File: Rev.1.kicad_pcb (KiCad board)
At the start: 4 copper layers, 238.3 x 170.8 mm, 228 parts, among them J1 Power from PowerBoard, J10 UnitV02, J11 GH-S37D, J12 NeoPixel, J13 LoadCell, J14 NeoPixel, J15 LoadCell, J16 Power to TopBoard, J17 Comm to TopBoard, J18 Conn_01x08_Socket, J19 ST-Link, J2 Power from PowerBoard, J20 USB_C_Receptacle_USB2.0_16P, J21 ST-Link, J22 to TopBoard, J23 LIDAR, J24 ST-Link, J25 to TopBoard, J26 Power to TopBoard, J27 Power to TopBoard, J28 Power to TopBoard, J29 Power from BackBoard, J3 ST-Link, J4 Power from PowerBoard, J5 Com from BackBoard, J6 to TileBoard, J7 to LidarBoard, J8 UnitV01, J9 GH-S37D, M1 STS3032, M2 STS3032, M3 STS3032, M4 STS3032, Q1 BSS138, Q2 BSS138, Q3 BSS138, Q4 BSS138, Q5 TJ15S06M3L, Q6 BSS138, Q7 BSS138, Q8 BSS138, SW1 RESET_SWITCH, SW10 MODE_SWITCH, SW11 TC-06104-043E, SW12 TC-06104-043E, SW2 MODE_SWITCH, SW3 GW-12LWP, SW4 RESET_SWITCH, SW5 MODE_SWITCH, SW6 START_SWITCH, SW7 RESET_SWITCH, SW8 MODE_SWITCH, SW9 RESET_SWITCH, U1 VL53L0X, U10 VL53L0X, U11 VL53L0X, U12 STM32F446RET6, U13 Sit2001B, U14 STM32F446RET6, U15 MAX3485, U16 Sit2001B, U17 RT9080-33GJ5, U18 Sit2001B, U19 STM32F446RET6, U2 Sit2001B, U20 S11059, U21 LT1085CM-3.3#PBF, U22 CH340E, U3 VL53L0X, U4 STM32H747IGT6, U5 AE-BNO055-BO, U6 NJU77551F, U7 NJU77551F, U8 MIC5219-5.0YM5-TR, U9 AZ1117CH-3.3TRG1

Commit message: LiDAR基板Rev.2修正
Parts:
- added J30: BNO055, Connector_PinSocket_1.27mm:PinSocket_1x02_P1.27mm_Vertical, F.Cu at (71.8, 132.5)
- added J31: UNITV, Connector_PinSocket_1.27mm:PinSocket_1x02_P1.27mm_Vertical, F.Cu at (66.8, 132.5)
- added J32: UNITV, Connector_PinSocket_1.27mm:PinSocket_1x02_P1.27mm_Vertical, F.Cu at (46.2, 122.3)
- added J33: to TileBoard, Connector_PinSocket_1.27mm:PinSocket_1x02_P1.27mm_Vertical, F.Cu at (56.9, 129.1)
- added J34: SERVO, Connector_PinSocket_1.27mm:PinSocket_1x02_P1.27mm_Vertical, F.Cu at (53.8, 111.4)
- added J35: NeoPixel, Connector_PinSocket_1.27mm:PinSocket_1x02_P1.27mm_Vertical, F.Cu at (46.2, 117.6)
- added R34: 680, Resistor_SMD:R_0603_1608Metric, F.Cu at (154.5, 135.3)
- added R48: 10k, Resistor_SMD:R_0603_1608Metric, F.Cu at (198.5, 146.0)
- added U23: AE-BNO055-BO, AE-BNO055-BO:AE-BNO055-BO, F.Cu at (125.7, 134.6)
- C43, R21, R22, SW4, SW5: moved to F.Cu
- moved SW4 102.6 mm to (251.6, 138.9), turned to 0 degrees
- moved J21 96.2 mm to (215.4, 154.9), turned to -90 degrees
- moved C43 95.0 mm to (247.8, 139.3)
- moved R22 88.8 mm to (244.1, 142.0), turned to 180 degrees
- moved SW5 82.5 mm to (240.9, 138.1), turned to 0 degrees
- moved R21 75.8 mm to (237.6, 142.0), turned to 180 degrees
- moved SW8 55.0 mm to (240.7, 146.5)
- moved R28 52.4 mm to (237.1, 150.8)
- moved R29 44.9 mm to (244.2, 151.0), turned to 180 degrees
- moved C51 43.2 mm to (322.2, 141.0), turned to -90 degrees
- moved SW7 41.7 mm to (251.8, 146.7)
- moved C50 40.6 mm to (318.7, 152.2), turned to 180 degrees
- moved C54 36.6 mm to (247.5, 146.8), turned to -90 degrees
- moved C56 34.5 mm to (316.8, 154.3)
- moved U14 33.9 mm to (313.4, 144.2)
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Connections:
- C58 pad 2: Net-(U22-VCC) -> Net-(U22-V3)
- SW11 pad 2: Net-(U19-PC6) -> Net-(U19-PB12)
- SW12 pad 2: Net-(U19-PC7) -> Net-(U19-PB13)
- U14 pad 21: unconnected-(U14-PA5-Pad21) -> /Back/SCK
- U14 pad 22: unconnected-(U14-PA6-Pad22) -> /Back/MOSI
- U14 pad 23: unconnected-(U14-PA7-Pad23) -> /Back/MISO
- U14 pad 41: unconnected-(U14-PA8-Pad41) -> /Back/CS
- U19 pad 22: unconnected-(U19-PA6-Pad22) -> /Lidar/PWM
- U19 pad 23: unconnected-(U19-PA7-Pad23) -> /Lidar/PWM2
- U19 pad 33: unconnected-(U19-PB12-Pad33) -> Net-(U19-PB12)
- U19 pad 34: unconnected-(U19-PB13-Pad34) -> Net-(U19-PB13)
- U19 pad 35: unconnected-(U19-PB14-Pad35) -> /Lidar/IN2
- U19 pad 36: unconnected-(U19-PB15-Pad36) -> /Lidar/IN3
- U19 pad 37: Net-(U19-PC6) -> /Lidar/TX6
- U19 pad 38: Net-(U19-PC7) -> /Lidar/RX6
- U19 pad 40: unconnected-(U19-PC9-Pad40) -> /Lidar/SDA2
- U19 pad 41: unconnected-(U19-PA8-Pad41) -> /Lidar/SCL2
- U19 pad 53: unconnected-(U19-PC12-Pad53) -> /Lidar/TX5
- U19 pad 54: unconnected-(U19-PD2-Pad54) -> /Lidar/RX5
- U19 pad 58: unconnected-(U19-PB6-Pad58) -> /Lidar/SCL
- U19 pad 59: unconnected-(U19-PB7-Pad59) -> /Lidar/SDA
- U22 pad 10: +5V -> Net-(U22-V3)
- U22 pad 7: Net-(U22-VCC) -> +5V
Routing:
- net Net-(M1-S): track 184.2 -> 0.00 mm
- net +3.3V: track 494.3 -> 374.4 mm, vias 72 -> 53
- net GND: track 694.0 -> 585.1 mm, vias 512 -> 432
- net /Back/NRST: track 108.4 -> 0.00 mm, vias 3 -> 0
- net /Back/SDA: track 98.4 -> 0.00 mm
- net +7.5V: track 416.9 -> 332.7 mm, vias 5 -> 0
- net /Back/SCL: track 77.3 -> 0.00 mm
- net Net-(SW5A-B): track 62.8 -> 0.00 mm, vias 2 -> 0
- net Net-(BT1-+): track 66.5 -> 8.54 mm, vias 1 -> 0
- net +5V: track 632.9 -> 586.0 mm, vias 14 -> 10
- net /Back/XSHUT2: track 43.9 -> 0.00 mm
- net /Back/XSHUT1: track 33.1 -> 0.00 mm, vias 1 -> 0
- net /Back/TX3: track 32.1 -> 0.00 mm, vias 2 -> 0
- net /Back/DIN: track 32.0 -> 0.00 mm
- net /Back/PC2: track 30.1 -> 0.00 mm, vias 2 -> 0
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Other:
- board text added: "BNO055"
- board text added: "C"
- board text added: "D"
- board text added: "NeoPixel"
- board text added: "R"
- board text added: "SERVO"
- board text added: "T"
- board text added: "Tile"
- board text added: "UNITV"

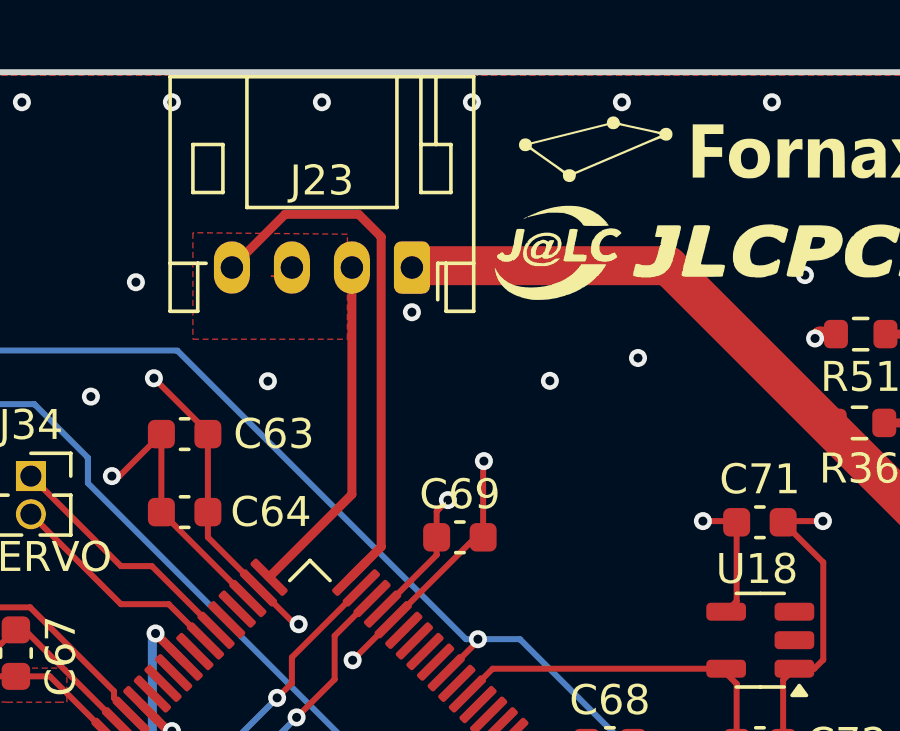
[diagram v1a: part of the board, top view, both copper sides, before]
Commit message: LiDAR基板Rev.2修正v2
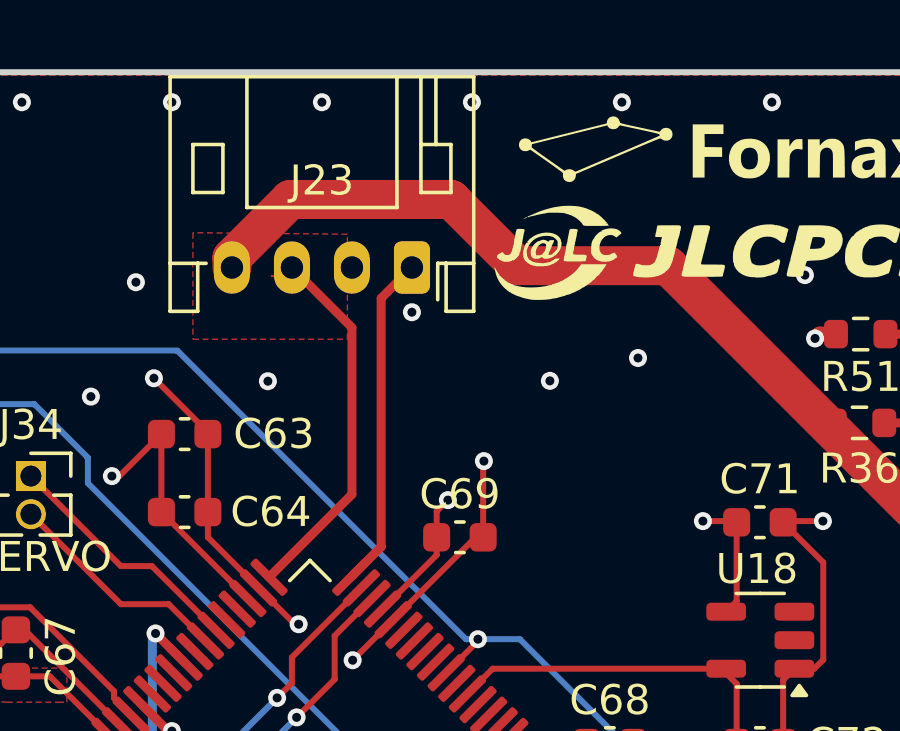
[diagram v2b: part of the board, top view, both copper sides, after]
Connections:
- J23 pad 1: +5V -> /Lidar/TX2
- J23 pad 2: /Lidar/RX2 -> GND
- J23 pad 3: GND -> /Lidar/RX2
- J23 pad 4: /Lidar/TX2 -> +5V
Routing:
- net +5V: track 586.0 -> 594.6 mm
- net /Lidar/TX2: track 18.1 -> 11.2 mm
- net /Lidar/RX2: track 11.6 -> 12.5 mm
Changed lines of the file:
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@@
 			(remove_unused_layers no)
 			(roundrect_rratio 0.208333)
-			(net 4 "+5V")
+			(net 17 "/Lidar/TX2")
 			(pinfunction "Pin_1")
 			(pintype "passive")
@@
 			(layers "*.Cu" "*.Mask")
 			(remove_unused_layers no)
-			(net 18 "/Lidar/RX2")
+			(net 3 "GND")
 			(pinfunction "Pin_2")
 			(pintype "passive")
@@
 			(layers "*.Cu" "*.Mask")
 			(remove_unused_layers no)
-			(net 3 "GND")
+			(net 18 "/Lidar/RX2")
 			(pinfunction "Pin_3")
 			(pintype "passive")
@@
 			(layers "*.Cu" "*.Mask")
 			(remove_unused_layers no)
-			(net 17 "/Lidar/TX2")
+			(net 4 "+5V")
 			(pinfunction "Pin_4")
 			(pintype "passive")
@@
 	)
 	(segment
+		(start 75.039666 104.387132)
+		(end 70.017132 104.387132)
+		(width 1.3)
+		(layer "F.Cu")
+		(net 4)
+	)
+	(segment
 		(start 40.780367 137.306717)
 		(end 40.780367 138.777632)
@@
 	)
 	(segment
-		(start 93.250367 137.729132)
-		(end 93.250367 121.687132)
-		(width 1.3)
-		(layer "F.Cu")
-		(net 4)
-	)
-	(segment
-		(start 93.250367 121.687132)
-		(end 86.263235 114.7)
-		(width 1.3)
-		(layer "F.Cu")
-		(net 4)
-	)
-	(segment
 		(start 90.5 180.05)
 		(end 91.3 180.85)
@@
 	)
 	(segment
+		(start 93.208367 137.729132)
+		(end 93.250367 137.729132)
+		(width 1.3)
+		(layer "F.Cu")
+		(net 4)
+	)
+	(segment
 		(start 64.075367 140.437132)
 		(end 64.075367 139.910526)
@@
 	)
 	(segment
-		(start 75.039666 104.387132)
-		(end 66.560367 104.387132)
+		(start 93.250367 121.687132)
+		(end 86.263235 114.7)
 		(width 1.3)
 		(layer "F.Cu")
@@
 	)
 	(segment
-		(start 56.573 64.778)
-		(end 56.4665 64.8845)
-		(width 1.5)
+		(start 60.410367 104.387132)
+		(end 60.560367 104.387132)
+		(width 0.3)
 		(layer "F.Cu")
 		(net 4)
 	)
 	(segment
-		(start 93.208367 137.729132)
-		(end 93.250367 137.729132)
+		(start 70.017132 104.387132)
+		(end 67.81 102.18)
 		(width 1.3)
 		(layer "F.Cu")
@@
 	)
 	(segment
+		(start 56.573 64.778)
+		(end 56.4665 64.8845)
+		(width 1.5)
+		(layer "F.Cu")
+		(net 4)
+	)
+	(segment
 		(start 48.687867 127.362133)
 		(end 48.687867 131.02)
@@
 	)
 	(segment
+		(start 93.250367 137.729132)
+		(end 93.250367 121.687132)
+		(width 1.3)
+		(layer "F.Cu")
+		(net 4)
+	)
+	(segment
 		(start 230.35 74.35)
 		(end 230.35 75.6)
@@
 	)
 	(segment
+		(start 60.500367 104.887132)
+		(end 60.500367 104.597128)
+		(width 0.2)
+		(layer "F.Cu")
+		(net 4)
+	)
+	(segment
 		(start 53.9655 65.8125)
 		(end 53.0375 64.8845)
@@
 	)
 	(segment
+		(start 60.500367 104.121522)
+		(end 60.500367 104.447132)
+		(width 1.3)
+		(layer "F.Cu")
+		(net 4)
+	)
+	(segment
 		(start 62.8125 65.8125)
 		(end 72.5725 75.5725)
@@
 	)
 	(segment
+		(start 65.300367 145.037132)
+		(end 85.900367 145.037132)
+		(width 1.3)
+		(layer "F.Cu")
+		(net 4)
+	)
+	(segment
 		(start 50.650367 131.024632)
 		(end 48.692499 131.024632)
@@
 	)
 	(segment
+		(start 67.81 102.18)
+		(end 62.441889 102.18)
+		(width 1.3)
+		(layer "F.Cu")
+		(net 4)
+	)
+	(segment
 		(start 253.745 63.345)
 		(end 254.1 63.7)
@@
 	)
 	(segment
+		(start 62.441889 102.18)
+		(end 60.500367 104.121522)
+		(width 1.3)
+		(layer "F.Cu")
+		(net 4)
+	)
+	(segment
+		(start 85.352534 114.7)
+		(end 75.039666 104.387132)
+		(width 1.3)
+		(layer "F.Cu")
+		(net 4)
+	)
+	(segment
 		(start 48.687867 131.02)
 		(end 48.687867 133.912867)
@@
 	)
 	(segment
-		(start 65.300367 145.037132)
-		(end 85.900367 145.037132)
-		(width 1.3)
-		(layer "F.Cu")
-		(net 4)
-	)
-	(segment
 		(start 91.3 180.85)
 		(end 99.15 180.85)
@@
 	)
 	(segment
-		(start 86.263235 114.7)
-		(end 85.352534 114.7)
+		(start 85.900367 145.037132)
+		(end 93.208367 137.729132)
 		(width 1.3)
 		(layer "F.Cu")
@@
 	)
 	(segment
-		(start 85.900367 145.037132)
-		(end 93.208367 137.729132)
+		(start 86.263235 114.7)
+		(end 85.352534 114.7)
 		(width 1.3)
 		(layer "F.Cu")
@@
 	)
 	(segment
-		(start 85.352534 114.7)
-		(end 75.039666 104.387132)
-		(width 1.3)
-		(layer "F.Cu")
-		(net 4)
-	)
-	(segment
 		(start 84.975367 133.499632)
 		(end 84.975367 124.781371)
@@
 	)
 	(segment
-		(start 60.410367 104.387132)
-		(end 60.560367 104.387132)
+		(start 66.500367 104.447132)
+		(end 65.475367 105.472132)
 		(width 0.3)
 		(layer "F.Cu")
@@
 	)
 	(segment
-		(start 64.725367 102.674632)
-		(end 65.475367 103.424632)
-		(width 0.3)
-		(layer "F.Cu")
-		(net 17)
-	)
-	(segment
-		(start 62.272867 102.674632)
-		(end 64.725367 102.674632)
-		(width 0.3)
-		(layer "F.Cu")
-		(net 17)
-	)
-	(segment
-		(start 60.560367 104.387132)
-		(end 62.272867 102.674632)
+		(start 65.475367 105.472132)
+		(end 65.475367 113.758832)
 		(width 0.3)
 		(layer "F.Cu")
@@
 	)
 	(segment
-		(start 60.500367 104.887132)
-		(end 60.500367 104.597128)
-		(width 0.2)
-		(layer "F.Cu")
-		(net 17)
-	)
-	(segment
 		(start 65.475367 113.758832)
 		(end 64.461548 114.772651)
@@
 	)
 	(segment
-		(start 65.475367 103.424632)
-		(end 65.475367 113.758832)
+		(start 62.650367 104.297132)
+		(end 62.500367 104.447132)
 		(width 0.3)
 		(layer "F.Cu")
-		(net 17)
+		(net 18)
 	)
 	(segment
-		(start 64.500367 104.447132)
-		(end 64.500367 112.01147)
+		(start 62.500367 104.447132)
+		(end 64.500367 106.447132)
 		(width 0.3)
 		(layer "F.Cu")
@@
 	)
 	(segment
-		(start 64.500367 104.297132)
-		(end 64.500367 104.447132)
+		(start 64.500367 106.447132)
+		(end 64.500367 112.01147)
 		(width 0.3)
 		(layer "F.Cu")

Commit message: メイン基板Rev.2完成
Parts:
- removed the C18 at (225.5, 48.7)
- removed the C19 at (225.5, 44.7)
- removed the C22 at (225.5, 32.5)
- removed the C23 at (189.1, 56.7)
- removed the C24 at (186.6, 56.7)
- removed the C25 at (158.8, 77.5)
- removed the C26 at (186.6, 52.6)
- removed the C27 at (189.1, 52.6)
- removed the C30 at (201.9, 27.5)
- removed the C31 at (222.2, 27.5)
- removed the J12 at (255.8, 49.5)
- removed the J14 at (158.0, 49.5)
- removed the Q3 at (254.7, 56.8)
- removed the Q4 at (161.9, 55.2)
- removed Q7: BSS138, Package_TO_SOT_SMD:SOT-23
- removed the R10 at (255.2, 53.5)
- removed the R15 at (156.8, 55.5)
- removed the R16 at (167.2, 51.7)
- removed the R23 at (255.4, 122.2)
- removed the R9 at (257.3, 60.0)
- removed the SW6 at (245.6, 126.6)
- removed the U10 at (181.6, 150.3)
- added D4: LED, LED_SMD:LED_0603_1608Metric, F.Cu at (208.9, 154.5)
- added G***: LOGO, icon:fornax-logo-pcb15-3.8, F.Cu at (167.2, 23.4)
- added G***: LOGO, icon:jlcpcb-logo-pcb15-8, F.Cu at (167.2, 26.7)
- added Q5: BSS138, Package_TO_SOT_SMD:SOT-23, F.Cu at (261.7, 120.7)
- added R18: 470, Resistor_SMD:R_0603_1608Metric, F.Cu at (205.3, 154.6)
- added R19: 1k, Resistor_SMD:R_0603_1608Metric, F.Cu at (167.9, 141.3)
- added R25: 10k, Capacitor_SMD:C_0603_1608Metric_Pad1.08x0.95mm_HandSolder, F.Cu at (257.1, 122.0)
- added SW3: B-12CCP, B-12CCP:B-12CCP, F.Cu at (172.3, 136.7)
- added U13: ~, Connector_PinSocket_2.54mm:PinSocket_1x06_P2.54mm_Vertical, F.Cu at (234.8, 160.5)
- added U7: MOUDLE-SEEEDUINO-XIAO-ESP32C3, XIAO:MOUDLE14P-SMD-2.54-21X17.8MM, F.Cu at (269.0, 64.3)
- C1, C15: value 0.1uF -> 1uF
- C14: value 0.1uF -> 4.7uF
- C20, C21: value 0.1uF -> 2.2uF
- FB1: footprint Capacitor_SMD:C_0603_1608Metric -> Inductor_SMD:L_0603_1608Metric
- J11, J9: footprint Connector_PinHeader_2.54mm:PinHeader_1x03_P2.54mm_Vertical -> Connector_JST:JST_ZH_B3B-ZR_1x03_P1.50mm_Vertical
- J6: moved to B.Cu
- R1, R2: footprint Resistor_SMD:R_0603_1608Metric -> Capacitor_SMD:C_0603_1608Metric_Pad1.08x0.95mm_HandSolder
- R26: value 10k -> 1k; footprint Capacitor_SMD:C_0603_1608Metric_Pad1.08x0.95mm_HandSolder -> Resistor_SMD:R_0603_1608Metric
- R3: value 10k -> 47
- R31, R32, U5: moved to F.Cu
- R4: value 0 -> 10k; footprint Resistor_SMD:R_0603_1608Metric -> Capacitor_SMD:C_0603_1608Metric_Pad1.08x0.95mm_HandSolder
- SW6: renamed from SW3; value GW-12LWP -> B-12CCP; footprint GW-12LWP:GW-12LWP -> B-12CCP:B-12CCP
- U1, U11, U3: value VL53L0X -> ~; footprint Connector_PinHeader_2.54mm:PinHeader_1x05_P2.54mm_Vertical -> Connector_PinSocket_2.54mm:PinSocket_1x06_P2.54mm_Vertical
- U4: value STM32H747IGT6 -> STM32H723ZGTx; footprint Package_QFP:LQFP-176_24x24mm_P0.5mm -> Package_QFP:LQFP-144_20x20mm_P0.5mm
- moved U3 123.9 mm to (273.1, 76.1), turned to 180 degrees
- moved U1 118.3 mm to (149.0, 63.5), turned to 0 degrees
- moved R2 108.1 mm to (256.1, 23.4), turned to 180 degrees
- moved SW1 106.8 mm to (252.8, 36.4)
- moved C47 106.4 mm to (196.6, 107.5)
- moved U17 106.4 mm to (196.5, 111.3)
- moved C42 106.1 mm to (202.7, 112.4), turned to 180 degrees
- moved C45 106.0 mm to (196.6, 114.7)
- moved SW2 105.8 mm to (252.7, 28.2), turned to 0 degrees
- moved C39 105.4 mm to (208.3, 125.9)
- moved C43 105.4 mm to (207.8, 109.0)
- moved C40 105.4 mm to (216.8, 125.3)
- moved C41 105.4 mm to (220.3, 114.1)
- moved C37 105.4 mm to (207.9, 105.8)
- moved C38 105.4 mm to (202.5, 118.9)
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- renumbered C28 to C18, C29 to C19, C32 to C22, C33 to C23, C34 to C24, C35 to C25, C36 to C26, C37 to C27, C38 to C28, C39 to C29, C40 to C30, C41 to C31, C42 to C32, C43 to C33, C44 to C34, C45 to C35, C46 to C36, C47 to C37, C48 to C38, C49 to C39, C50 to C40, C51 to C41, C52 to C42, C53 to C43, C54 to C44, C55 to C45, C59 to C46, C57 to C47, C56 to C48, C63 to C49, C64 to C50, C65 to C51, C66 to C52, C67 to C53, C68 to C54, C69 to C55, C62 to C56, C61 to C57, C70 to C58, C60 to C59, C58 to C60, C71 to C61, C73 to C62, C72 to C63, C74 to C64, C75 to C65, C76 to C66, C77 to C67, C78 to C68, D8 to D10, D9 to D11, D10 to D12, D11 to D13, D4 to D5, D5 to D6, D6 to D7, D7 to D8, D12 to D9, J13 to J12, J15 to J13, J16 to J14, J17 to J15, J18 to J16, J19 to J17, J21 to J18, J24 to J19, J22 to J20, J20 to J21, J23 to J22, J30 to J23, J31 to J24, J33 to J25, J32 to J26, J34 to J27, J35 to J28, J25 to J29, J26 to J30, J27 to J31, J28 to J32, J29 to J33, MD2 to MD1, Q5 to Q3, Q6 to Q4, Q8 to Q6, R12 to R10, R13 to R11, R14 to R12, R17 to R13, R18 to R14, R19 to R15, R20 to R16, R48 to R17, R21 to R20, R22 to R21, R34 to R22, R25 to R23, R35 to R34, R36 to R35, R37 to R36, R38 to R37, R49 to R38, R50 to R39, R51 to R40, R39 to R41, R40 to R42, R41 to R43, R42 to R44, R43 to R45, R44 to R46, R45 to R47, R46 to R48, R47 to R49, R11 to R9, U9 to U10, U23 to U12, U12 to U14, U13 to U15, U14 to U16, U16 to U17, U15 to U18, U17 to U19, U22 to U20, U19 to U21, U18 to U22, U20 to U23, U21 to U24, U7 to U8, U8 to U9
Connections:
- C15 pad 1: +3.3V -> VDDA
- C16 pad 1: +3.3V -> VDDA
- C17 pad 1: +3.3V -> GND
- C17 pad 2: GND -> /Top/NRST
- C20 pad 1: +3.3V -> GND
- C20 pad 2: GND -> Net-(C20-Pad2)
- C21 pad 1: +3.3V -> GND
- C21 pad 2: GND -> Net-(C21-Pad2)
- J22 pad 1: /Lidar/TX2 -> +5V
- J22 pad 2: GND -> /Lidar/RX2
- J22 pad 3: /Lidar/RX2 -> GND
- J22 pad 4: +5V -> /Lidar/TX2
- Q3 pad 2: Net-(Q5-G) -> Net-(Q3-G)
- R1 pad 2: Net-(U4-PDR_ON) -> Net-(SW2A-A)
- R17 pad 1: Net-(Q5-G) -> Net-(Q3-G)
- R2 pad 1: +3.3V -> GND
- R2 pad 2: Net-(SW2A-A) -> Net-(SW2A-C)
- R23 pad 2: Net-(SW6A-A) -> Net-(R23-Pad2)
- R24 pad 1: +3.3V -> +5V
- R26 pad 1: GND -> Net-(R26-Pad1)
- R26 pad 2: Net-(SW6A-C) -> +7.5V
- R3 pad 1: GND -> VDDA
- R3 pad 2: Net-(SW2A-C) -> Net-(U4-VREF+)
- R4 pad 1: VDDA -> +3.3V
- R4 pad 2: Net-(U4-VREF+) -> Net-(U4-PDR_ON)
- R7 pad 2: /Top/DIN1 -> Net-(D1-DIN)
- R8 pad 2: Net-(D1-DIN) -> /Top/DIN1
- SW6 pad 1: Net-(Q5-G) -> Net-(R23-Pad2)
- SW6 pad 2: GND -> Net-(SW6-B)
- SW6 pad 3: unconnected-(SW3A-C-Pad3) -> GND
- U1 pad 1: /Top/XSHUT1 -> unconnected-(U1-GPIO1-Pad1)
- U1 pad 2: +3.3V -> /Top/XSHUT1
- U1 pad 3: GND -> +3.3V
- U1 pad 4: /Top/SDA -> GND
- U1 pad 5: /Top/SCL -> /Top/SDA
- U11 pad 1: /Back/XSHUT1 -> unconnected-(U11-GPIO1-Pad1)
- U11 pad 2: +3.3V -> /Back/XSHUT2
- U11 pad 3: GND -> +3.3V
- U11 pad 4: /Back/SDA -> GND
- U11 pad 5: /Back/SCL -> /Back/SDA
- U14 pad 33: Net-(SW6A-B) -> Net-(SW6-B)
- U16 pad 26: unconnected-(U14-PB0-Pad26) (its old number) -> /Back/DC
- U16 pad 27: unconnected-(U14-PB1-Pad27) (its old number) -> /Back/PWM
- U16 pad 28: unconnected-(U14-PB2-Pad28) (its old number) -> /Back/DIN
- U3 pad 1: /Top/XSHUT2 -> unconnected-(U3-GPIO1-Pad1)
- U3 pad 2: +3.3V -> /Top/XSHUT2
- U3 pad 3: GND -> +3.3V
- U3 pad 4: /Top/SDA -> GND
- U3 pad 5: /Top/SCL -> /Top/SDA
- U4 pad 100: GND -> unconnected-(U4-PA8-Pad100)
- U4 pad 101: +3.3V -> unconnected-(U4-PA9-Pad101)
- U4 pad 102: +3.3V -> unconnected-(U4-PA10-Pad102)
- U4 pad 103: GND -> unconnected-(U4-PA11-Pad103)
- U4 pad 104: GND -> unconnected-(U4-PA12-Pad104)
- U4 pad 105: GND -> /Top/SWDIO
- U4 pad 106: GND -> Net-(C21-Pad2)
- U4 pad 109: GND -> /Top/SWCLK
- U4 pad 112: GND -> unconnected-(U4-PC11-Pad112)
- U4 pad 113: +3.3V -> unconnected-(U4-PC12-Pad113)
- U4 pad 119: GND -> unconnected-(U4-PD5-Pad119)
- U4 pad 12: GND -> unconnected-(U4-PF2-Pad12)
- U4 pad 120: unconnected-(U4-VDD50_USB-Pad120) -> GND
- U4 pad 121: GND -> +3.3V
- U4 pad 122: /Top/TX6 -> unconnected-(U4-PD6-Pad122)
- U4 pad 123: /Top/RX6 -> unconnected-(U4-PD7-Pad123)
- U4 pad 126: +3.3V -> unconnected-(U4-PG11-Pad126)
- U4 pad 13: +3.3V -> unconnected-(U4-PF3-Pad13)
- U4 pad 130: unconnected-(U4-PA11-Pad130) -> GND
- U4 pad 131: unconnected-(U4-PA12-Pad131) -> +3.3V
- U4 pad 132: /Top/SWDIO -> unconnected-(U4-PG15-Pad132)
- U4 pad 133: Net-(C30-Pad2) -> unconnected-(U4-PB3(JTDO-Pad133)
- U4 pad 134: GND -> unconnected-(U4-PB4(NJTRST)-Pad134)
- U4 pad 135: +3.3V -> unconnected-(U4-PB5-Pad135)
- U4 pad 136: +3.3V -> unconnected-(U4-PB6-Pad136)
- U4 pad 137: GND -> unconnected-(U4-PB7-Pad137)
- U4 pad 138: /Top/SWCLK -> Net-(SW2A-B)
- U4 pad 14: GND -> unconnected-(U4-PF4-Pad14)
- U4 pad 143: unconnected-(U4-PD0-Pad143) -> Net-(U4-PDR_ON)
- U4 pad 144: unconnected-(U4-PD1-Pad144) -> +3.3V
- U4 pad 15: GND -> unconnected-(U4-PF5-Pad15)
- U4 pad 17: GND -> +3.3V
- U4 pad 18: unconnected-(U4-PF0-Pad18) -> /Top/RX7
- U4 pad 19: unconnected-(U4-PF1-Pad19) -> /Top/TX7
- U4 pad 23: unconnected-(U4-PF5-Pad23) -> /Top/HSE
- U4 pad 24: GND -> unconnected-(U4-PH1-Pad24)
- U4 pad 25: +3.3V -> /Top/NRST
- U4 pad 28: /Top/DIN3 -> unconnected-(U4-PC2_C-Pad28)
- U4 pad 30: unconnected-(U4-PF10-Pad30) -> +3.3V
- U4 pad 31: /Top/HSE -> GND
- U4 pad 32: unconnected-(U4-PH1-Pad32) -> Net-(U4-VREF+)
- U4 pad 33: /Top/NRST -> VDDA
- U4 pad 34: unconnected-(U4-PC0-Pad34) -> /Top/TX4
- U4 pad 35: unconnected-(U4-PC1-Pad35) -> /Top/RX4
- U4 pad 36: unconnected-(U4-PC2_C-Pad36) -> /Top/TX2
- U4 pad 37: unconnected-(U4-PC3_C-Pad37) -> /Top/RX2
- U4 pad 39: Net-(U4-VREF+) -> +3.3V
- U4 pad 40: VDDA -> unconnected-(U4-PA4-Pad40)
- U4 pad 41: /Top/TX4 -> /Top/PWM2
- U4 pad 42: /Top/RX4 -> /Top/DIN1
- U4 pad 43: /Top/TX2 -> unconnected-(U4-PA7-Pad43)
- U4 pad 44: +3.3V -> /Top/AD1
- U4 pad 45: GND -> unconnected-(U4-PC5-Pad45)
- U4 pad 46: /Top/RX2 -> unconnected-(U4-PB0-Pad46)
- U4 pad 47: GND -> unconnected-(U4-PB1-Pad47)
- U4 pad 48: +3.3V -> unconnected-(U4-PB2-Pad48)
- U4 pad 49: unconnected-(U4-PA4-Pad49) -> /Top/AD2
- U4 pad 50: /Top/PWM2 -> unconnected-(U4-PF12-Pad50)
- U4 pad 51: /Top/DIN1 -> GND
- U4 pad 52: unconnected-(U4-PA7-Pad52) -> +3.3V
- U4 pad 53: /Top/AD1 -> /Top/AD3
- U4 pad 54: unconnected-(U4-PC5-Pad54) -> /Top/SCL
- U4 pad 55: unconnected-(U4-PB0-Pad55) -> /Top/SDA
- U4 pad 56: unconnected-(U4-PB1-Pad56) -> /Top/XSHUT1
- U4 pad 57: unconnected-(U4-PB2-Pad57) -> /Top/XSHUT2
- U4 pad 58: /Top/AD3 -> unconnected-(U4-PE7-Pad58)
- U4 pad 6: GND -> +3.3V
- U4 pad 60: /Top/AD2 -> /Top/PWM1
- U4 pad 61: /Top/SCL -> GND
- U4 pad 62: /Top/SDA -> +3.3V
- U4 pad 63: /Top/XSHUT1 -> unconnected-(U4-PE10-Pad63)
- U4 pad 64: GND -> unconnected-(U4-PE11-Pad64)
- U4 pad 65: +3.3V -> unconnected-(U4-PE12-Pad65)
- U4 pad 66: /Top/XSHUT2 -> unconnected-(U4-PE13-Pad66)
- U4 pad 69: /Top/PWM1 -> /Top/RX3
- U4 pad 7: +3.3V -> unconnected-(U4-PC13-Pad7)
- U4 pad 70: GND -> /Top/TX3
- U4 pad 71: +3.3V -> Net-(C20-Pad2)
- U4 pad 72: unconnected-(U4-PE10-Pad72) -> +3.3V
- U4 pad 73: unconnected-(U4-PE11-Pad73) -> /Top/RX5
- U4 pad 74: unconnected-(U4-PE12-Pad74) -> /Top/TX5
- U4 pad 75: unconnected-(U4-PE13-Pad75) -> /Top/TX1
- U4 pad 76: unconnected-(U4-PE14-Pad76) -> /Top/RX1
- U4 pad 78: /Top/RX3 -> unconnected-(U4-PD9-Pad78)
- U4 pad 79: /Top/TX3 -> unconnected-(U4-PD10-Pad79)
- U4 pad 8: +3.3V -> unconnected-(U4-PC14-Pad8)
- U4 pad 80: Net-(C30-Pad2) -> unconnected-(U4-PD11-Pad80)
- U4 pad 81: GND -> unconnected-(U4-PD12-Pad81)
- U4 pad 82: +3.3V -> unconnected-(U4-PD13-Pad82)
- U4 pad 85: /Top/RX5 -> unconnected-(U4-PD14-Pad85)
- U4 pad 86: /Top/TX5 -> unconnected-(U4-PD15-Pad86)
- U4 pad 87: /Top/TX1 -> unconnected-(U4-PG2-Pad87)
- U4 pad 88: /Top/RX1 -> unconnected-(U4-PG3-Pad88)
- U4 pad 92: +3.3V -> unconnected-(U4-PG7-Pad92)
- U4 pad 93: GND -> unconnected-(U4-PG8-Pad93)
- U4 pad 94: unconnected-(U4-PD11-Pad94) -> GND
- U4 pad 95: /Top/DIN2 -> +3.3V
- U4 pad 96: unconnected-(U4-PD13-Pad96) -> /Top/TX6
- U4 pad 97: unconnected-(U4-PD14-Pad97) -> /Top/RX6
- U4 pad 99: +3.3V -> unconnected-(U4-PC9-Pad99)
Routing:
- net GND: track 585.1 -> 471.3 mm, vias 432 -> 467
- net /Top/RX7: track 0.00 -> 78.4 mm, vias 0 -> 2
- net +3.3V: track 374.4 -> 300.7 mm, vias 53 -> 40
- net /Top/TX7: track 0.00 -> 63.5 mm, vias 0 -> 2
- net Net-(C30-Pad2): track 60.7 -> 0.00 mm, vias 2 -> 0
- net /Top/DIN2: track 43.3 -> 0.00 mm, vias 2 -> 0
- net /Top/DIN3: track 43.0 -> 0.00 mm, vias 2 -> 0
- net /Top/NRST: track 72.3 -> 113.6 mm, vias 1 -> 4
- net +5V: track 594.6 -> 559.3 mm
- net /Top/TX2: track 16.9 -> 43.0 mm
- net /Top/SCL: track 152.9 -> 177.4 mm, vias 1 -> 2
- net /Top/RX2: track 13.8 -> 35.9 mm
- net /Top/PWM1: track 44.1 -> 65.0 mm, vias 0 -> 1
- net /Top/SWDIO: track 88.5 -> 108.9 mm
- net /Top/SDA: track 153.8 -> 173.0 mm
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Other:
- board size 238.3 x 170.8 mm -> 245.3 x 171.4 mm
- board text added: "BACK"
- board text added: "POWER"
- board text added: "START"
- board text added: "UI"
